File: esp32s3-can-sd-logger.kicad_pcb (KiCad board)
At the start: 4 copper layers, 84 x 100 mm, 206 parts, among them J1 PWR + CAN harness, J10 Sensor harness, J2 USB-C, J3 UART0, J4 I2C / Qwiic, J5 SPI, J6 WS2812, J7 Spare IO, J8 Rail break-out, J9 microSD push-pull, Q1 IPD068N10, Q2 AO3401A, Q3 2N7002, Q4 AO3401A, Q5 MMBT3906, Q6 DMG2301L, Q7 2N7002, SW1 RESET, SW2 BOOT, U1 LM74700-Q1, U10 SRV05-4, U11 SRV05-4, U12 TJA1051T/3, U13 ADS1115, U2 TLV431A, U3 LM5164 (5V), U4 LM5164 (3V3), U5 ESP32-S3-WROOM-1-N16R8, U6 TLV431A, U7 USBLC6-2SC6, U8 USBLC6-2SC6, U9 74AHCT1G125

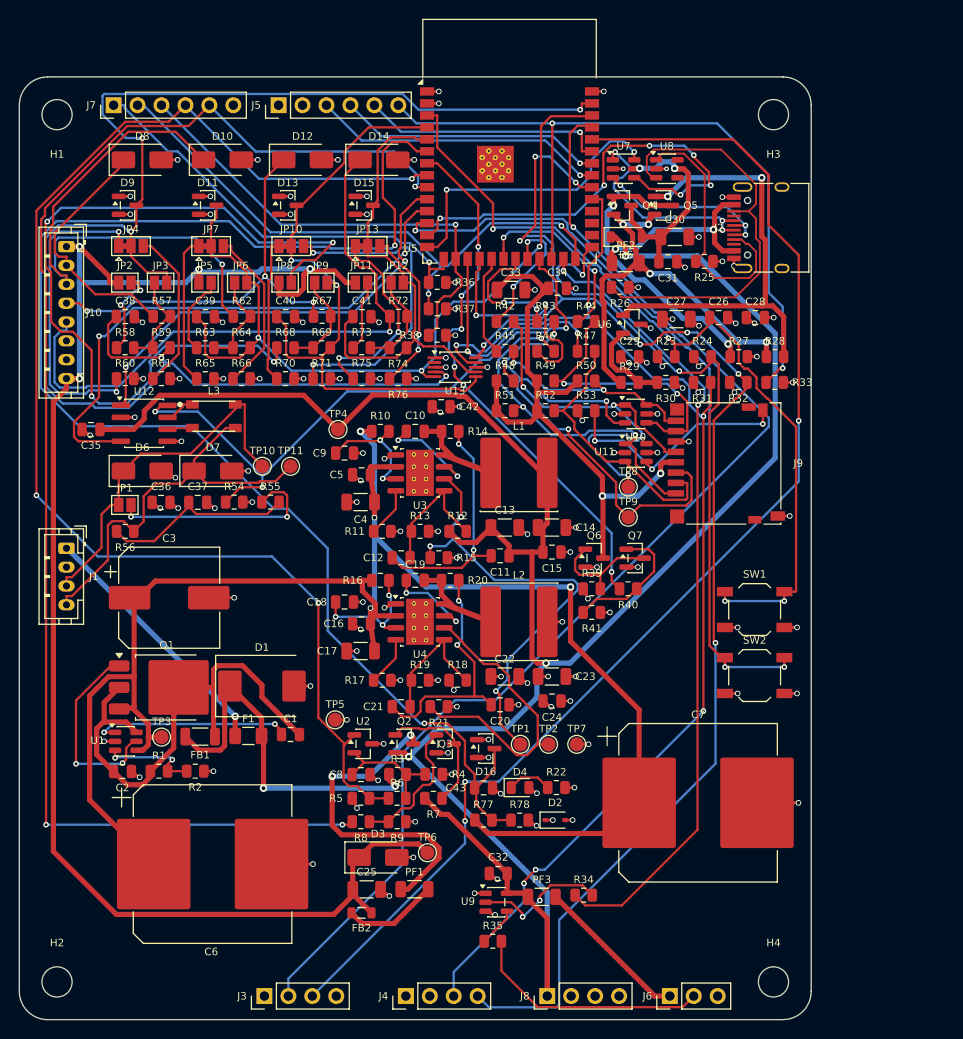
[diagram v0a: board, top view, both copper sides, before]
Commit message: Re-scope the fork as a carrier board: no power section, differential analog, K-line
The shield idea does not survive measurement. Component courtyard on the
parent is 3052 mm2 over an 84 x 100 board -- 36% packing, not the 50% I had
been estimating -- and a DevKitC-1 is 63 x 25.5 = 1607 mm2. The parts alone
were 1.4x the whole dev board. So this is a carrier the dev board plugs into,
not a shield that fits on top of one.

Power section deleted entirely. It was 1746 mm2, 57% of the board, for two
rails the DevKitC-1 already makes from its USB-C. Gone: both LM5164 bucks and
everything around them, the LM74700 ideal diode, the reverse-battery FET, the
three electrolytic cans, the 12 V input, and the sensor-rail load switch.
Both rails are now inputs, taken up through the sockets -- which reverses the
earlier "feed 5 V only" rule, because there is no longer a second regulator
to parallel against.

Hold-up is a supercapacitor, not electrolytics. The first sizing was wrong:
energy goes as V-squared and the usable window at 5 V is 4.2 -> 3.6 V, so
2000 uF buys 12.5 ms, not the ~50 ms claimed. 0.5 F over the same window is
2.5 s, in less area than one of the 100 V cans it replaces. Low-ESR
cylindrical cells specifically -- coin EDLCs are 30-200 ohm and cannot source
120 mA at all.

Analog runs differentially. The board is grounded twice now, through the
sensor loom and through USB by way of a charger elsewhere in the car, and a
few hundred mV of chassis drop is 6% of a 0-5 V channel -- which makes the
0.1% dividers pointless. The correction has to be at the divider, not the
ADC, so the sensor ground comes back as a Kelvin wire through a matched
attenuator. Two ADS1115s, because one MUX only offers three channels against
a shared negative.

K-line added, discrete rather than an L9637D: that part's TXD threshold is
0.7*VCC = 3.5 V and a 3.3 V GPIO cannot meet it. Low-side 2N7002, clamped
22k/10k receiver, optional ISO 9141 tester pull-up on a jumper.

Pin map regrouped by boa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
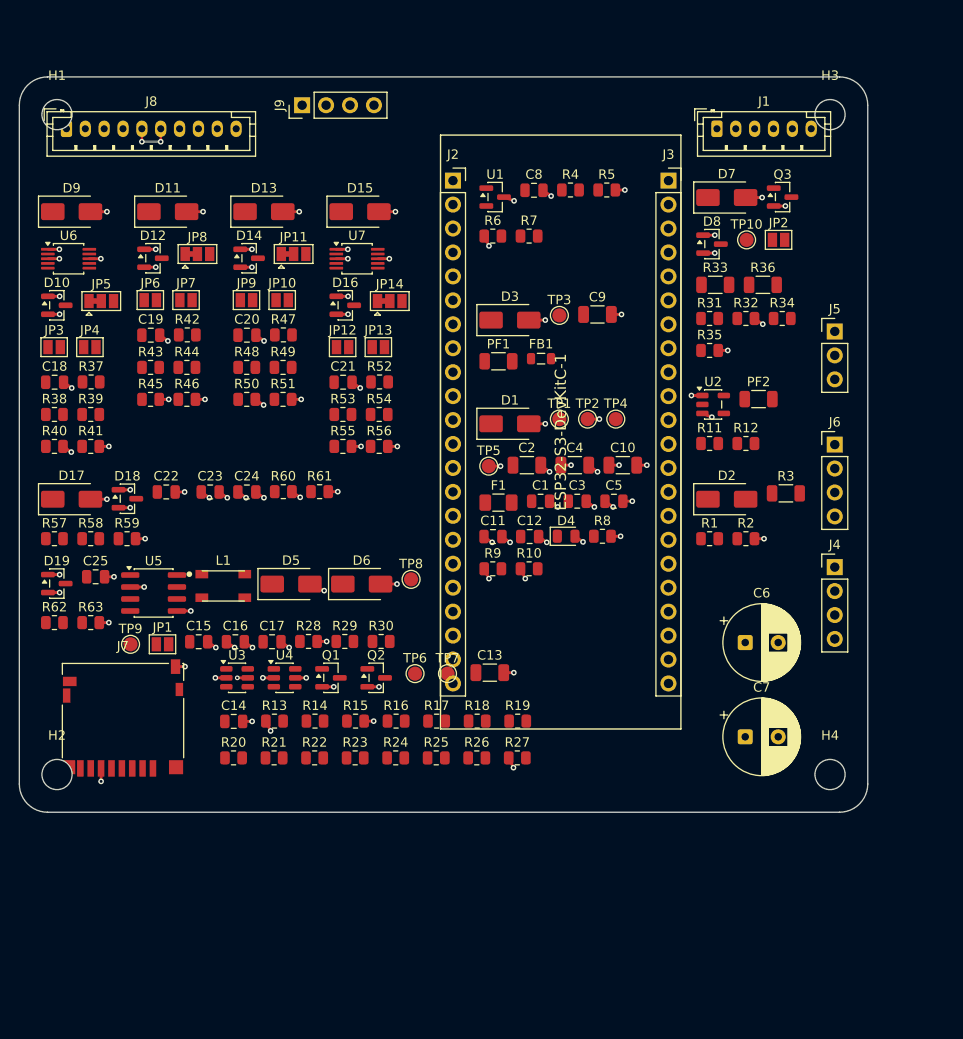
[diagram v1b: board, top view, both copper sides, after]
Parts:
- removed C26: 1uF, C_0805_2012Metric
- removed C27, C30, C33: 10uF, C_1206_3216Metric
- removed C28, C29, C31, C32, C34, C35, C36, C38, C39, C40, C41, C42, C43: 100nF, C_0805_2012Metric
- removed C37: 4.7nF, C_0805_2012Metric
- removed FB2: 600R, L_0805_2012Metric
- removed J10: Sensor harness, JST_PH_B8B-PH-K_1x08_P2.00mm_Vertical
- removed L2: 22uH, L_Sunlord_SWPA8040S
- removed L3: 51uH, L_CommonMode_TDK_ACT45B
- removed PF3: 0.5A hold, R_1206_3216Metric
- removed Q4: AO3401A, SOT-23
- removed Q5: MMBT3906, SOT-23
- removed Q6: DMG2301L, SOT-23
- removed Q7: 2N7002, SOT-23
- removed R64, R69, R74: 10k, R_0805_2012Metric
- removed R65, R70, R75: 15k, R_0805_2012Metric
- removed R66, R71, R76: 2.21k, R_0805_2012Metric
- removed R67, R72: 1k, R_0805_2012Metric
- removed R68, R73: 2.49k, R_0805_2012Metric
- removed R77: 100k, R_0805_2012Metric
- removed R78: 8.2k, R_0805_2012Metric
- removed SW1: RESET, SW_SPST_TL3342
- removed SW2: BOOT, SW_SPST_TL3342
- removed TP11: CAN_L, TestPoint_Pad_D1.5mm
- removed U10, U11: SRV05-4, SOT-23-6
- removed U12: TJA1051T/3, SOIC-8_3.9x4.9mm_P1.27mm
- removed U13: ADS1115, VSSOP-10_3x3mm_P0.5mm
- removed U8: USBLC6-2SC6, SOT-23-6
- removed U9: 74AHCT1G125, SOT-23-5
- added D17: SMAJ40CA, D_SMA, F.Cu at (5.54, 44.8)
- added D18: BAT54S, SOT-23, F.Cu at (11.5, 44.7)
- added D19: BAT54S, SOT-23, F.Cu at (3.98, 53.7)
- added JP14: RANGE4 (default 0-5V), SolderJumper-3_P1.3mm_Bridged12_Pad1.0x1.5mm, F.Cu at (39.3, 23.8)
- C1: value 1uF -> 100nF
- C10: value 2.2nF -> 10uF; footprint C_0805_2012Metric -> C_1206_3216Metric
- C11, C19, C20: value 2.2nF -> 100nF
- C12, C21: value 270pF -> 100nF
- C13: value 22uF -> 10uF
- C14, C22, C23: value 22uF -> 100nF; footprint C_1206_3216Metric -> C_0805_2012Metric
- C17: value 10uF -> 4.7nF; footprint C_1206_3216Metric -> C_0805_2012Metric
- C18: value 10nF -> 100nF
- C2: value 100nF -> 22uF; footprint C_0805_2012Metric -> C_1206_3216Metric
- C25: value 10uF -> 100nF; footprint C_1206_3216Metric -> C_0805_2012Metric
- C3: value 100uF -> 100nF; footprint CP_Elec_10x10.5 -> C_0805_2012Metric
- C4: value 10uF -> 22uF
- C6, C7: value 330uF -> 1F; footprint CP_Elec_16x22 -> CP_Radial_D8.0mm_P3.50mm
- C9: value 10nF -> 10uF; footprint C_0805_2012Metric -> C_1206_3216Metric
- D1: value SMCJ40CA -> SMAJ26CA; footprint D_SMC -> D_SMA
- D10, D12, D14, D8: value SMAJ40CA -> BAT54S; footprint D_SMA -> SOT-23
- D11, D13, D15, D9: value BAT54S -> SMAJ40CA; footprint SOT-23 -> D_SMA
- D2: value 3.6V 300mW -> SS14; footprint D_SOD-323 -> D_SMA
- D5: value 40V 1A -> SMAJ26CA; footprint D_SOD-123 -> D_SMA
- F1: value 2A slow -> 0.5A slow
- FB1: footprint L_1206_3216Metric -> L_0805_2012Metric
- J1: value PWR + CAN harness -> OBD-II harness; footprint JST_PH_B4B-PH-K_1x04_P2.00mm_Vertical -> JST_PH_B6B-PH-K_1x06_P2.00mm_Vertical
- J2: value USB-C -> DevKit J1; footprint USB_C_Receptacle_HRO_TYPE-C-31-M-12 -> PinSocket_1x22_P2.54mm_Vertical
- J3: value UART0 -> DevKit J3; footprint PinHeader_1x04_P2.54mm_Vertical -> PinSocket_1x22_P2.54mm_Vertical
- J5: value SPI -> WS2812; footprint PinHeader_1x06_P2.54mm_Vertical -> PinHeader_1x03_P2.54mm_Vertical
- J6: value WS2812 -> Rail break-out; footprint PinHeader_1x03_P2.54mm_Vertical -> PinHeader_1x04_P2.54mm_Vertical
- J7: value Spare IO -> microSD push-pull; footprint PinHeader_1x06_P2.54mm_Vertical -> microSD_HC_Hirose_DM3D-SF
- J8: value Rail break-out -> Sensor harness; footprint PinHeader_1x04_P2.54mm_Vertical -> JST_PH_B10B-PH-K_1x10_P2.00mm_Vertical
- J9: value microSD push-pull -> Spare diff in; footprint microSD_HC_Hirose_DM3D-SF -> PinHeader_1x04_P2.54mm_Vertical
- JP10: value RANGE3 (default 0-5V) -> BYPASS3; footprint SolderJumper-3_P1.3mm_Bridged12_Pad1.0x1.5mm -> SolderJumper-2_P1.3mm_Open_Pad1.0x1.5mm
- JP11: value PULLUP4 -> RANGE3 (default 0-5V); footprint SolderJumper-2_P1.3mm_Open_Pad1.0x1.5mm -> SolderJumper-3_P1.3mm_Bridged12_Pad1.0x1.5mm
- JP12: value BYPASS4 -> PULLUP4
- JP13: value RANGE4 (default 0-5V) -> BYPASS4; footprint SolderJumper-3_P1.3mm_Bridged12_Pad1.0x1.5mm -> SolderJumper-2_P1.3mm_Open_Pad1.0x1.5mm
- JP2: value PULLUP1 -> KPU (default OFF)
- JP3: value BYPASS1 -> PULLUP1
- JP4: value RANGE1 (default 0-5V) -> BYPASS1; footprint SolderJumper-3_P1.3mm_Bridged12_Pad1.0x1.5mm -> SolderJumper-2_P1.3mm_Open_Pad1.0x1.5mm
- JP5: value PULLUP2 -> RANGE1 (default 0-5V); footprint SolderJumper-2_P1.3mm_Open_Pad1.0x1.5mm -> SolderJumper-3_P1.3mm_Bridged12_Pad1.0x1.5mm
- JP6: value BYPASS2 -> PULLUP2
- JP7: value RANGE2 (default 0-5V) -> BYPASS2; footprint SolderJumper-3_P1.3mm_Bridged12_Pad1.0x1.5mm -> SolderJumper-2_P1.3mm_Open_Pad1.0x1.5mm
- JP8: value PULLUP3 -> RANGE2 (default 0-5V); footprint SolderJumper-2_P1.3mm_Open_Pad1.0x1.5mm -> SolderJumper-3_P1.3mm_Bridged12_Pad1.0x1.5mm
- JP9: value BYPASS3 -> PULLUP3
- L1: value 33uH -> 51uH; footprint L_Sunlord_SWPA8040S -> L_CommonMode_TDK_ACT45B
- Q1: value IPD068N10 -> DMG2301L; footprint TO-252-3_TabPin2 -> SOT-23
- Q2: value AO3401A -> 2N7002
- R10, R9: value 100k -> 4.7k
- R11: value 31.6k -> 33
- R12: value 100k -> 100
- R13: value 31.6k -> 100k
- R14: value 121k -> 1k
- R16, R18, R21: value 100k -> 33
- R17: value 20.5k -> 33
- R19: value 57.6k -> 33
- R2: value 44.2k -> 100k
- R20: value 95.3k -> 33
- R22: value 1k -> 10k
- R25, R26: value 5.1k -> 10k
- R27: value 100k -> 47k
- R29: value 100k -> 60.4
- R3: value 100k -> 22; footprint R_0805_2012Metric -> R_1206_3216Metric
- R30: value 27.4k -> 60.4
- R31: value 4.7k -> 10k
- R32: value 4.7k -> 100k
- R33: value 10k -> 33; footprint R_0805_2012Metric -> R_1206_3216Metric
- R34: value 33 -> 22k
- R35: value 100 -> 10k
- R36: value 10k -> 510; footprint R_0805_2012Metric -> R_1206_3216Metric
- R37, R52, R8: value 10k -> 1k
- R38, R48: value 10k -> 2.49k
- R39: value 100k -> 10k
- R4: value 12.7k -> 28.7k
- R40: value 1k -> 15k
- R41: value 100k -> 2.21k
- R42, R47: value 33 -> 1k
- R43: value 33 -> 2.49k
- R44: value 33 -> 10k
- R45: value 33 -> 15k
- R46: value 33 -> 2.21k
- R5: value 10k -> 12.0k
- R50, R59: value 10k -> 15k
- R51: value 10k -> 2.21k
- R53: value 47k -> 2.49k
- R55: value 60.4 -> 15k
- R56: value 60.4 -> 2.21k
- R58: value 2.49k -> 10k
- R6: value 1M -> 10k
- R60: value 15k -> 100k
- R61: value 2.21k -> 100k
- R62: value 1k -> 100k
- R63: value 2.49k -> 8.2k
- R7: value 100k -> 1M
- TP1: value PG_5V -> +5V
- TP10: value CAN_H -> K_LINE
- TP2: value PG_3V3 -> +3V3
- TP3: value +VBAT -> +5VS
- TP4: value +5V -> OBD_VBAT
- TP5: value +3V3 -> GND
- TP6: value +5VS -> SD_CLK
- TP7: value GND -> SD_CMD
- TP8: value SD_CLK -> CAN_H
- TP9: value SD_CMD -> CAN_L
- U1: value LM74700-Q1 -> TLV431A; footprint SOT-23-6 -> SOT-23
- U2: value TLV431A -> 74AHCT1G125; footprint SOT-23 -> SOT-23-5
- U3: value LM5164 (5V) -> SRV05-4; footprint SOIC-8-1EP_3.9x4.9mm_P1.27mm_EP2.95x4.9mm_Mask2.71x3.4mm_ThermalVias -> SOT-23-6
- U4: value LM5164 (3V3) -> SRV05-4; footprint SOIC-8-1EP_3.9x4.9mm_P1.27mm_EP2.95x4.9mm_Mask2.71x3.4mm_ThermalVias -> SOT-23-6
- U5: value ESP32-S3-WROOM-1-N16R8 -> TJA1051T/3; footprint ESP32-S3-WROOM-1 -> SOIC-8_3.9x4.9mm_P1.27mm
- U6: value TLV431A -> ADS1115 (0x48); footprint SOT-23 -> VSSOP-10_3x3mm_P0.5mm
- U7: value USBLC6-2SC6 -> ADS1115 (0x49); footprint SOT-23-6 -> VSSOP-10_3x3mm_P0.5mm
- moved J8 105.2 mm to (5.00, 5.50), turned to 0 degrees
- moved J3 96.5 mm to (68.9, 11.0), turned to 0 degrees
- moved J1 82.1 mm to (74.0, 5.50), turned to 0 degrees
- moved U1 69.8 mm to (50.5, 12.7)
- moved R5 69.6 mm to (62.3, 12.0)
- moved JP2 69.5 mm to (80.5, 17.3)
- moved Q3 68.2 mm to (81.0, 12.7)
- moved R35 66.8 mm to (73.2, 29.0)
- moved J7 65.0 mm to (11.0, 68.0), turned to 0 degrees
- moved R34 64.7 mm to (80.9, 25.6)
- moved C8 64.6 mm to (54.6, 12.0)
- moved J4 64.3 mm to (86.5, 52.0), turned to 0 degrees
- moved J5 63.7 mm to (86.5, 27.0), turned to 0 degrees
- moved R4 63.7 mm to (58.5, 12.0)
- moved R2 63.4 mm to (77.1, 49.0)
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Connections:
- C1 pad 1: VCAP -> OBD_VBAT_F
- C1 pad 2: VBAT_FB -> GND
- C10 pad 1: BST_5V -> +3V3
- C10 pad 2: SW_5V -> GND
- C11 pad 1: RAMP_5V -> +3V3
- C11 pad 2: +5V -> GND
- C12 pad 1: RAMP_5V -> +5V
- C12 pad 2: FB_5V -> GND
- C13 pad 1: +5V -> SD_VDD
- C14 pad 1: +5V -> SD_VDD
- C16 pad 1: +VBAT -> +3V3
- C17 pad 1: +VBAT -> CAN_SPLIT
- C18 pad 1: EN_3V3 -> AIN1
- C19 pad 1: BST_3V3 -> AIN2
- C19 pad 2: SW_3V3 -> GND
- C2 pad 1: VBAT_FB -> +5V
- C20 pad 1: RAMP_3V3 -> AIN3
- C20 pad 2: +3V3 -> GND
- C21 pad 1: RAMP_3V3 -> AIN4
- C21 pad 2: FB_3V3 -> GND
- C22 pad 1: +3V3 -> AGND_SENSE
- C25 pad 1: +5VS -> VBAT_SNS
- C3 pad 1: +VBAT -> +5V
- C4 pad 1: +VBAT -> +3V3
- C5 pad 1: +VBAT -> +3V3
- C6 pad 1: +VBAT -> SCAP_TOP
- C6 pad 2: GND -> SCAP_MID
- C7 pad 1: +VBAT -> SCAP_MID
- C9 pad 1: EN_5V -> +5VS
- D1 pad 1: VBAT_F -> OBD_VBAT_F
- D10 pad 1: AIN2_IN -> GND
- D10 pad 2: GND -> +3V3
- D11 pad 1: GND -> AIN2_IN
- D11 pad 2: +3V3 -> GND
- D12 pad 1: AIN3_IN -> GND
- D12 pad 2: GND -> +3V3
- D13 pad 1: GND -> AIN3_IN
- D13 pad 2: +3V3 -> GND
- D14 pad 1: AIN4_IN -> GND
- D14 pad 2: GND -> +3V3
- D15 pad 1: GND -> AIN4_IN
- D15 pad 2: +3V3 -> GND
- D16 pad 3: VBAT_SNS -> AIN4
- D2 pad 1: +3V3 -> SCAP_TOP
- D2 pad 2: GND -> +5V
- D5 pad 1: +5V -> CAN_H
- D5 pad 2: VBUS -> GND
- D6 pad 1: CAN_H -> CAN_L
- D7 pad 1: CAN_L -> K_LINE
- D8 pad 1: AIN1_IN -> GND
- D8 pad 2: GND -> +3V3
- D9 pad 1: GND -> AIN1_IN
- D9 pad 2: +3V3 -> GND
- F1 pad 1: VBAT_IN -> OBD_VBAT
- F1 pad 2: VBAT_F -> OBD_VBAT_F
- FB1 pad 1: VBAT_F -> VSENS_F
- FB1 pad 2: VBAT_FB -> +5VS
- J1 pad 1: VBAT_IN -> OBD_VBAT
- J3 pad 1: +3V3 -> GND
- J3 pad 2: UART_TX -> (no net)
- J3 pad 3: UART_RX -> (no net)
- J3 pad 4: GND -> (no net)
- J5 pad 1: +3V3 -> LED_5V
- J5 pad 2: GND -> LED_DIN_J
- J5 pad 3: SPI_SCK -> GND
- J6 pad 1: LED_5V -> +5V
- J6 pad 2: LED_DIN_J -> +3V3
- J7 pad 1: IO3 -> SD_D2_C
- J7 pad 2: IO45 -> SD_D3_C
- J7 pad 3: IO46 -> SD_CMD_C
- J7 pad 4: PWR_FAIL -> SD_VDD
- J7 pad 5: SENS_EN -> SD_CLK_C
- J8 pad 1: +5V -> +5VS
- J8 pad 2: +3V3 -> +5VS
- J8 pad 3: GND -> AIN1_IN
- J8 pad 4: GND -> AIN2_IN
- J9 pad 1: SD_D2_C -> AIN_SP1
- J9 pad 2: SD_D3_C -> AIN_SP2
- J9 pad 3: SD_CMD_C -> AGND_SENSE
- J9 pad 4: SD_VDD -> GND
- JP10 pad 1: AIN3_R1 -> AIN3_A
- JP11 pad 1: +5VS -> AIN3_R1
- JP11 pad 2: AIN4_PU -> AIN3
- JP12 pad 1: AIN4_A -> +5VS
- JP12 pad 2: AIN4 -> AIN4_PU
- JP13 pad 1: AIN4_R1 -> AIN4_A
- JP2 pad 1: +5VS -> OBD_VBAT_F
- JP2 pad 2: AIN1_PU -> K_PU
- JP3 pad 1: AIN1_A -> +5VS
- JP3 pad 2: AIN1 -> AIN1_PU
- JP4 pad 1: AIN1_R1 -> AIN1_A
- JP5 pad 1: +5VS -> AIN1_R1
- JP5 pad 2: AIN2_PU -> AIN1
- JP6 pad 1: AIN2_A -> +5VS
- JP6 pad 2: AIN2 -> AIN2_PU
- JP7 pad 1: AIN2_R1 -> AIN2_A
- JP8 pad 1: +5VS -> AIN2_R1
- JP8 pad 2: AIN3_PU -> AIN2
- JP9 pad 1: AIN3_A -> +5VS
- JP9 pad 2: AIN3 -> AIN3_PU
- L1 pad 1: SW_5V -> CANH_T
- L1 pad 2: +5V -> CAN_H
- PF1 pad 1: VSENS_SW -> +5V
- PF2 pad 1: VBUS_IN -> +5V
- PF2 pad 2: VBUS_R -> LED_5V
- Q1 pad 1: GATE_RB -> SD_PG
- Q1 pad 2: VBAT_FB -> +3V3
- Q1 pad 3: +VBAT -> SD_VDD
- Q2 pad 1: SENS_G -> SD_EN_G
- Q2 pad 2: +5V -> GND
- Q2 pad 3: VSENS_SW -> SD_PG
- Q3 pad 1: SENS_EN_G -> K_TX_G
- Q3 pad 3: SENS_G -> K_TX_D
- R1 pad 1: VBAT_FB -> SCAP_TOP
- R1 pad 2: VBAT_UVLO -> SCAP_MID
- R10 pad 1: +VBAT -> +3V3
- R10 pad 2: EN_5V -> I2C_SCL
- R11 pad 1: RON_5V -> LED_DIN_MCU
- R11 pad 2: GND -> LED_DIN_A
- R12 pad 1: +5V -> LED_DIN
- R12 pad 2: FB_5V -> LED_DIN_J
- R13 pad 1: FB_5V -> +3V3
- R13 pad 2: GND -> SD_PG
- R14 pad 1: SW_5V -> SD_PWR_EN
- R14 pad 2: RAMP_5V -> SD_EN_G
- R15 pad 1: PG_5V -> SD_EN_G
- R15 pad 2: +3V3 -> GND
- R16 pad 1: +VBAT -> SD_CLK
- R16 pad 2: EN_3V3 -> SD_CLK_C
- R17 pad 1: RON_3V3 -> SD_CMD
- R17 pad 2: GND -> SD_CMD_C
- R18 pad 1: +3V3 -> SD_D0
- R18 pad 2: FB_3V3 -> SD_D0_C
- R19 pad 1: FB_3V3 -> SD_D1
- R19 pad 2: GND -> SD_D1_C
- R2 pad 1: VBAT_UVLO -> SCAP_MID
- R20 pad 1: SW_3V3 -> SD_D2
- R20 pad 2: RAMP_3V3 -> SD_D2_C
- R21 pad 1: PG_3V3 -> SD_D3
- R21 pad 2: +3V3 -> SD_D3_C
- R22 pad 1: PWR_LED_K -> SD_VDD
- R22 pad 2: GND -> SD_CMD_C
- R23 pad 1: +3V3 -> SD_VDD
- R23 pad 2: MCU_EN -> SD_D0_C
- R24 pad 1: +3V3 -> SD_VDD
- R24 pad 2: MCU_BOOT -> SD_D1_C
- R25 pad 1: USB_CC1 -> SD_VDD
- R25 pad 2: GND -> SD_D2_C
- R26 pad 1: USB_CC2 -> SD_VDD
- R26 pad 2: GND -> SD_D3_C
- R27 pad 1: VBUS_G -> +3V3
- R27 pad 2: GND -> SD_CD
- R28 pad 1: VBUS_R -> CAN_S
- R28 pad 2: VBUS_OV -> GND
- R29 pad 1: VBUS_R -> TERM_A
- R29 pad 2: VBUS_OVS -> CAN_SPLIT
- R3 pad 1: VBAT_F -> +5V
- R3 pad 2: PFD_SENSE -> SCAP_TOP
- R30 pad 1: VBUS_OVS -> CAN_SPLIT
- R30 pad 2: GND -> CAN_L
- R31 pad 1: +3V3 -> K_TX
- R31 pad 2: I2C_SDA -> K_TX_G
- R32 pad 1: +3V3 -> K_TX_G
- R32 pad 2: I2C_SCL -> GND
- R33 pad 1: SPI_CS -> K_TX_D
- R33 pad 2: +3V3 -> K_LINE
- R34 pad 1: LED_DIN_MCU -> K_LINE
- R34 pad 2: LED_DIN_A -> K_RX
- R35 pad 1: LED_DIN -> K_RX
- R35 pad 2: LED_DIN_J -> GND
- R36 pad 1: IO3 -> K_PU
- R36 pad 2: GND -> K_LINE
- R37 pad 1: IO45 -> AIN1_IN
- R37 pad 2: GND -> AIN1_A
- R38 pad 1: IO46 -> AIN1_PU
- R38 pad 2: GND -> AIN1_A
- R39 pad 1: +3V3 -> AIN1_A
- R39 pad 2: SD_PG -> AIN1
- R4 pad 1: PFD_SENSE -> +5V
- R4 pad 2: GND -> PFD_SENSE
- R40 pad 1: SD_PWR_EN -> AIN1_R1
- R40 pad 2: SD_EN_G -> GND
- R41 pad 1: SD_EN_G -> AIN1_R2
- R42 pad 1: SD_CLK -> AIN2_IN
- R42 pad 2: SD_CLK_C -> AIN2_A
- R43 pad 1: SD_CMD -> AIN2_PU
- R43 pad 2: SD_CMD_C -> AIN2_A
- R44 pad 1: SD_D0 -> AIN2_A
- R44 pad 2: SD_D0_C -> AIN2
- R45 pad 1: SD_D1 -> AIN2_R1
- R45 pad 2: SD_D1_C -> GND
- R46 pad 1: SD_D2 -> AIN2_R2
- R46 pad 2: SD_D2_C -> GND
- R47 pad 1: SD_D3 -> AIN3_IN
- R47 pad 2: SD_D3_C -> AIN3_A
- R48 pad 1: SD_VDD -> AIN3_PU
- R48 pad 2: SD_CMD_C -> AIN3_A
- R49 pad 1: SD_VDD -> AIN3_A
- R49 pad 2: SD_D0_C -> AIN3
- R5 pad 1: +3V3 -> PFD_SENSE
- R5 pad 2: PWR_FAIL -> GND
- R50 pad 1: SD_VDD -> AIN3_R1
- R50 pad 2: SD_D1_C -> GND
- R51 pad 1: SD_VDD -> AIN3_R2
- R51 pad 2: SD_D2_C -> GND
- R52 pad 1: SD_VDD -> AIN4_IN
- R52 pad 2: SD_D3_C -> AIN4_A
- R53 pad 1: +3V3 -> AIN4_PU
- R53 pad 2: SD_CD -> AIN4_A
- R54 pad 1: CAN_S -> AIN4_A
- R54 pad 2: GND -> AIN4
- R55 pad 1: TERM_A -> AIN4_R1
- R55 pad 2: CAN_SPLIT -> GND
- R56 pad 1: CAN_SPLIT -> AIN4_R2
- R56 pad 2: CAN_L -> GND
- R57 pad 1: AIN1_IN -> SENS_RTN
- R57 pad 2: AIN1_A -> AGND_A
- R58 pad 1: AIN1_PU -> AGND_A
- R58 pad 2: AIN1_A -> AGND_SENSE
- R59 pad 1: AIN1_A -> AGND_SENSE
- R59 pad 2: AIN1 -> GND
- R6 pad 1: PWR_FAIL -> +3V3
- R6 pad 2: PFD_SENSE -> PWR_FAIL
- R60 pad 1: AIN1_R1 -> AIN_SP1
- R61 pad 1: AIN1_R2 -> AIN_SP2
- R62 pad 1: AIN2_IN -> OBD_VBAT
- R62 pad 2: AIN2_A -> VBAT_SNS
- R63 pad 1: AIN2_PU -> VBAT_SNS
- R63 pad 2: AIN2_A -> GND
- R7 pad 1: +5V -> PWR_FAIL
- R7 pad 2: SENS_G -> PFD_SENSE
- R8 pad 1: SENS_EN -> PWR_LED_K
- R8 pad 2: SENS_EN_G -> GND
- R9 pad 1: SENS_EN_G -> +3V3
- R9 pad 2: GND -> I2C_SDA
- TP1 pad 1: PG_5V -> +5V
- TP10 pad 1: CAN_H -> K_LINE
- TP2 pad 1: PG_3V3 -> +3V3
- TP3 pad 1: +VBAT -> +5VS
- TP4 pad 1: +5V -> OBD_VBAT
- TP5 pad 1: +3V3 -> GND
- TP6 pad 1: +5VS -> SD_CLK_C
- TP7 pad 1: GND -> SD_CMD_C
- TP8 pad 1: SD_CLK_C -> CAN_H
- TP9 pad 1: SD_CMD_C -> CAN_L
- U1 pad 1: VCAP -> PWR_FAIL
- U1 pad 2: GND -> PFD_SENSE
- U1 pad 3: VBAT_UVLO -> GND
- U2 pad 1: PWR_FAIL -> GND
- U2 pad 2: PFD_SENSE -> LED_DIN_A
- U3 pad 1: GND -> SD_CLK_C
- U3 pad 2: +VBAT -> GND
- U3 pad 3: EN_5V -> SD_CMD_C
- U3 pad 4: RON_5V -> SD_D0_C
- U3 pad 5: FB_5V -> +3V3
- U3 pad 6: PG_5V -> SD_D1_C
- U4 pad 1: GND -> SD_D2_C
- U4 pad 2: +VBAT -> GND
- U4 pad 3: EN_3V3 -> SD_D3_C
- U4 pad 4: RON_3V3 -> SD_CD
- U4 pad 5: FB_3V3 -> +3V3
- U4 pad 6: PG_3V3 -> (no net)
- U5 pad 1: GND -> CAN_TX
- U5 pad 2: +3V3 -> GND
- U5 pad 3: MCU_EN -> +5V
- U5 pad 4: AIN3 -> CAN_RX
- U5 pad 5: AIN4 -> +3V3
- U5 pad 6: VBAT_SNS -> CANL_T
- U5 pad 7: SD_PWR_EN -> CANH_T
- U5 pad 8: PWR_FAIL -> CAN_S
- U6 pad 1: VBUS_OV -> GND
- U6 pad 2: VBUS_OVS -> (no net)
- U7 pad 1: USB_DP_CON -> +3V3
- U7 pad 2: GND -> (no net)
- U7 pad 3: USB_DM_CON -> GND
- U7 pad 4: USB_DM -> AIN4
- U7 pad 5: VBUS -> AIN_SP1
- U7 pad 6: USB_DP -> AIN_SP2
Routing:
- net +5V: track 241.0 -> 0.00 mm, vias 3 -> 0
- net +VBAT: track 183.1 -> 0.00 mm, vias 4 -> 0
- net AIN1: track 165.7 -> 0.00 mm, vias 5 -> 0
- net +5VS: track 162.9 -> 0.00 mm, vias 4 -> 0
- net VBAT_SNS: track 153.9 -> 0.00 mm, vias 2 -> 0
- net SENS_EN: track 148.2 -> 0.00 mm, vias 3 -> 0
- net I2C_SCL: track 147.4 -> 0.00 mm, vias 8 -> 0
- net PWR_FAIL: track 141.3 -> 0.00 mm, vias 3 -> 0
- net UART_RX: track 132.2 -> 0.00 mm, vias 3 -> 0
- net I2C_SDA: track 127.8 -> 0.00 mm, vias 6 -> 0
- net UART_TX: track 127.2 -> 0.00 mm, vias 1 -> 0
- net MCU_EN: track 89.7 -> 0.00 mm, vias 4 -> 0
- net AIN2: track 88.7 -> 0.00 mm, vias 3 -> 0
- net AIN3_PU: track 86.4 -> 0.00 mm, vias 4 -> 0
- net LED_DIN_MCU: track 85.3 -> 0.00 mm, vias 2 -> 0
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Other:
- board size 84 x 100 mm -> 90 x 78 mm
- board text added: "ESP32-S3-DevKitC-1"

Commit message: Second CAN bus, single analog range, and three placement bugs the render caught
TWO CAN BUSES AT ONCE NEEDS A SECOND CONTROLLER. The ESP32-S3 has exactly
one TWAI peripheral. Two transceivers on it would give a bus you can pick at
runtime through the GPIO matrix, never two live at once, and the point of a
second bus is watching the powertrain and the body bus together. So the
second channel is an MCP2518FD on SPI (SOIC-14, KiCad ships the pin-compatible
MCP2517FD symbol) with its own 40 MHz crystal, its own TJA1051 -- same part
as CAN 1, so two positions on one BOM line -- choke, split termination and
clamps.

That cost five pins against two spare. The three came from dropping the
microSD to 1-bit SDMMC, which measurement says is free: the busiest case this
logger will see is ~128 kB/s against 1-bit's ~1500 kB/s, and bus width does
not touch the card's internal write stall, which is the only thing the
hold-up budget is actually sized around. The card keeps its D1/D2/D3
pull-ups because a card samples DAT3 at power-up and drops into SPI mode if
it finds it low -- they simply stop at the socket now.

Jumpers on the aux harness pins pick K-line or the second CAN pair, because
those two genuinely cannot share a wire: K-line idles at battery voltage and
a CAN transceiver biases its bus to 2.5 V. The clamps sit ahead of the
jumpers so the protection is the same either way, which also let the K-line
drop its own TVS. Default is K-line, which is what an R53 wants.

ANALOG DOWN TO ONE RANGE. The bypass and range-select jumpers are gone --
twelve jumpers and four resistors -- and every channel is a fixed 2.21/13.21
divider spanning 0-16 V, so a 5 V and a 12 V sensor both fit without
touching anything. Resolution was never the reason for a narrower range: a
5 V sensor lands at 0.836 V, which on a 16-bit ADS1115 is 6688 counts.

The real reason is the differential ground. A channel switched to 0-16 V
while the shared return attenuator stayed at the 0-5 V ratio subtracts
0.5769*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
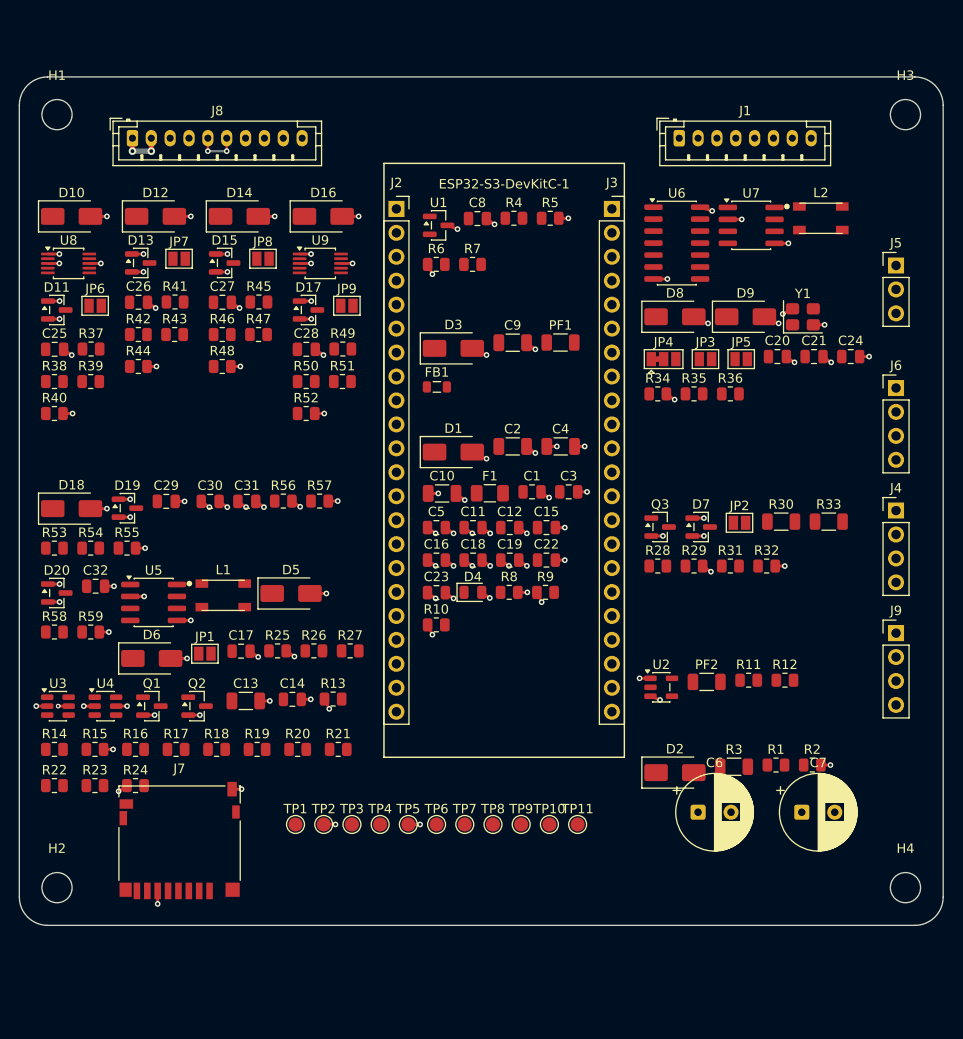
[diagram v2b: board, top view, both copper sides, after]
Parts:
- removed JP10: BYPASS3, SolderJumper-2_P1.3mm_Open_Pad1.0x1.5mm
- removed JP11: RANGE3 (default 0-5V), SolderJumper-3_P1.3mm_Bridged12_Pad1.0x1.5mm
- removed JP12: PULLUP4, SolderJumper-2_P1.3mm_Open_Pad1.0x1.5mm
- removed JP13: BYPASS4, SolderJumper-2_P1.3mm_Open_Pad1.0x1.5mm
- removed JP14: RANGE4 (default 0-5V), SolderJumper-3_P1.3mm_Bridged12_Pad1.0x1.5mm
- removed R60, R61, R62: 100k, R_0805_2012Metric
- removed R63: 8.2k, R_0805_2012Metric
- added C26: 100nF, C_0805_2012Metric, F.Cu at (12.6, 23.9)
- added C27: 100nF, C_0805_2012Metric, F.Cu at (21.5, 23.9)
- added C28: 100nF, C_0805_2012Metric, F.Cu at (30.4, 28.9)
- added C29: 100nF, C_0805_2012Metric, F.Cu at (15.6, 45.0)
- added C30: 100nF, C_0805_2012Metric, F.Cu at (20.2, 45.0)
- added C31: 100nF, C_0805_2012Metric, F.Cu at (24.1, 45.0)
- added C32: 100nF, C_0805_2012Metric, F.Cu at (8.10, 54.0)
- added D20: BAT54S, SOT-23, F.Cu at (3.98, 54.7)
- added L2: 51uH, L_CommonMode_TDK_ACT45B, F.Cu at (85.0, 15.0)
- added TP11: AUX_A, TestPoint_Pad_D1.5mm, F.Cu at (59.2, 79.3)
- added U8: ADS1115 (0x48), VSSOP-10_3x3mm_P0.5mm, F.Cu at (5.22, 19.8)
- added U9: ADS1115 (0x49), VSSOP-10_3x3mm_P0.5mm, F.Cu at (31.9, 19.8)
- added Y1: 40MHz, Crystal_SMD_3225-4Pin_3.2x2.5mm, F.Cu at (83.1, 25.4)
- C19: value 100nF -> 1uF
- C20, C21: value 100nF -> 15pF
- C24: value 100nF -> 4.7nF
- D10, D12, D14, D16, D18: value BAT54S -> SMAJ40CA; footprint SOT-23 -> D_SMA
- D11, D13, D15, D17: value SMAJ40CA -> BAT54S; footprint D_SMA -> SOT-23
- D7: value SMAJ26CA -> BAT54S; footprint D_SMA -> SOT-23
- D8: value BAT54S -> SMAJ26CA; footprint SOT-23 -> D_SMA
- D9: value SMAJ40CA -> SMAJ26CA
- J1: footprint JST_PH_B6B-PH-K_1x06_P2.00mm_Vertical -> JST_PH_B8B-PH-K_1x08_P2.00mm_Vertical
- JP3: value PULLUP1 -> TERM2 (default OFF)
- JP4: value BYPASS1 -> AUXSEL (default K-line); footprint SolderJumper-2_P1.3mm_Open_Pad1.0x1.5mm -> SolderJumper-3_P1.3mm_Bridged12_Pad1.0x1.5mm
- JP5: value RANGE1 (default 0-5V) -> AUXCL (default OFF); footprint SolderJumper-3_P1.3mm_Bridged12_Pad1.0x1.5mm -> SolderJumper-2_P1.3mm_Open_Pad1.0x1.5mm
- JP6: value PULLUP2 -> PULLUP1
- JP7: value BYPASS2 -> PULLUP2
- JP8: value RANGE2 (default 0-5V) -> PULLUP3; footprint SolderJumper-3_P1.3mm_Bridged12_Pad1.0x1.5mm -> SolderJumper-2_P1.3mm_Open_Pad1.0x1.5mm
- JP9: value PULLUP3 -> PULLUP4
- R19, R20, R21: value 33 -> 10k
- R24: value 10k -> 47k
- R26, R35: value 10k -> 60.4
- R27: value 47k -> 60.4
- R29: value 60.4 -> 100k
- R30: value 60.4 -> 33; footprint R_0805_2012Metric -> R_1206_3216Metric
- R31: value 10k -> 22k
- R32: value 100k -> 10k
- R33: value 33 -> 510
- R34: value 22k -> 10k
- R36: value 510 -> 60.4; footprint R_1206_3216Metric -> R_0805_2012Metric
- R40, R55: value 15k -> 2.21k
- R41: value 2.21k -> 1k
- R42: value 1k -> 2.49k
- R43: value 2.49k -> 10k
- R44: value 10k -> 2.21k
- R45: value 15k -> 1k
- R46: value 2.21k -> 2.49k
- R47: value 1k -> 10k
- R48: value 2.49k -> 2.21k
- R49: value 10k -> 1k
- R50: value 15k -> 2.49k
- R51: value 2.21k -> 10k
- R52: value 1k -> 2.21k
- R53: value 2.49k -> 1k
- R56: value 2.21k -> 100k
- R57: value 1k -> 100k
- R58: value 10k -> 100k
- R59: value 15k -> 8.2k
- U6: value ADS1115 (0x48) -> MCP2518FD; footprint VSSOP-10_3x3mm_P0.5mm -> SOIC-14_3.9x8.7mm_P1.27mm
- U7: value ADS1115 (0x49) -> TJA1051T/3; footprint VSSOP-10_3x3mm_P0.5mm -> SOIC-8_3.9x4.9mm_P1.27mm
- moved J9 84.3 mm to (93.0, 59.0), turned to 0 degrees
- moved D9 72.4 mm to (77.0, 25.4)
- moved JP3 69.1 mm to (72.8, 29.9)
- moved JP5 68.2 mm to (76.6, 29.9)
- moved C24 65.6 mm to (88.2, 29.7)
- moved TP10 65.4 mm to (56.2, 79.3)
- moved U6 64.5 mm to (69.7, 17.6)
- moved JP4 60.9 mm to (68.3, 29.9)
- moved TP3 58.3 mm to (35.3, 79.3)
- moved C20 56.3 mm to (80.4, 29.7)
- moved TP1 51.3 mm to (29.3, 79.3)
- moved TP2 51.3 mm to (32.3, 79.3)
- moved C21 50.0 mm to (84.3, 29.7)
- moved TP4 49.7 mm to (38.3, 79.3)
- moved C18 48.2 mm to (48.1, 51.3)
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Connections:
- C18 pad 1: AIN1 -> +3V3
- C19 pad 1: AIN2 -> +3V3
- C20 pad 1: AIN3 -> XTAL1
- C21 pad 1: AIN4 -> XTAL2
- C22 pad 1: AGND_SENSE -> +5V
- C24 pad 1: +3V3 -> CAN2_SPLIT
- C25 pad 1: VBAT_SNS -> AIN1
- D10 pad 1: GND -> AIN1_IN
- D10 pad 2: +3V3 -> GND
- D11 pad 1: AIN2_IN -> GND
- D11 pad 2: GND -> +3V3
- D12 pad 1: GND -> AIN2_IN
- D12 pad 2: +3V3 -> GND
- D13 pad 1: AIN3_IN -> GND
- D13 pad 2: GND -> +3V3
- D14 pad 1: GND -> AIN3_IN
- D14 pad 2: +3V3 -> GND
- D15 pad 1: AIN4_IN -> GND
- D15 pad 2: GND -> +3V3
- D16 pad 1: GND -> AIN4_IN
- D16 pad 2: +3V3 -> GND
- D17 pad 1: SENS_RTN -> GND
- D17 pad 2: GND -> +3V3
- D18 pad 1: GND -> SENS_RTN
- D18 pad 2: +3V3 -> GND
- D19 pad 3: VBAT_SNS -> AGND_SENSE
- D7 pad 1: K_LINE -> GND
- D7 pad 2: GND -> +3V3
- D8 pad 1: GND -> AUX_A
- D8 pad 2: +3V3 -> GND
- D9 pad 1: AIN1_IN -> AUX_B
- J1 pad 5: K_LINE -> AUX_A
- J1 pad 6: GND -> AUX_B
- J2 pad 15: SD_D3 -> I2C_SCL
- J2 pad 16: SD_D2 -> I2C_SDA
- J2 pad 17: SD_D1 -> SD_CD
- J3 pad 17: I2C_SDA -> SD_PWR_EN
- J3 pad 18: SD_CD -> CAN2_INT
- J3 pad 4: (no net) -> K_RX
- J3 pad 5: (no net) -> K_TX
- J3 pad 6: K_RX -> CAN2_CS
- J3 pad 7: K_TX -> CAN2_MISO
- J3 pad 8: SD_PWR_EN -> CAN2_MOSI
- J3 pad 9: I2C_SCL -> CAN2_SCK
- JP3 pad 1: +5VS -> CAN2_H_C
- JP3 pad 2: AIN1_PU -> TERM2_A
- JP4 pad 1: AIN1_A -> K_LINE
- JP4 pad 2: AIN1 -> AUX_A
- JP5 pad 1: AIN1_R1 -> AUX_B
- JP5 pad 2: AIN1 -> CAN2_L_C
- JP6 pad 2: AIN2_PU -> AIN1_PU
- JP7 pad 1: AIN2_A -> +5VS
- JP7 pad 2: AIN2 -> AIN2_PU
- JP8 pad 1: AIN2_R1 -> +5VS
- JP8 pad 2: AIN2 -> AIN3_PU
- JP9 pad 2: AIN3_PU -> AIN4_PU
- R19 pad 1: SD_D1 -> SD_VDD
- R19 pad 2: SD_D1_C -> SD_CMD_C
- R20 pad 1: SD_D2 -> SD_VDD
- R20 pad 2: SD_D2_C -> SD_D0_C
- R21 pad 1: SD_D3 -> SD_VDD
- R21 pad 2: SD_D3_C -> SD_D1_C
- R22 pad 2: SD_CMD_C -> SD_D2_C
- R23 pad 2: SD_D0_C -> SD_D3_C
- R24 pad 1: SD_VDD -> +3V3
- R24 pad 2: SD_D1_C -> SD_CD
- R25 pad 1: SD_VDD -> CAN_S
- R25 pad 2: SD_D2_C -> GND
- R26 pad 1: SD_VDD -> TERM_A
- R26 pad 2: SD_D3_C -> CAN_SPLIT
- R27 pad 1: +3V3 -> CAN_SPLIT
- R27 pad 2: SD_CD -> CAN_L
- R28 pad 1: CAN_S -> K_TX
- R28 pad 2: GND -> K_TX_G
- R29 pad 1: TERM_A -> K_TX_G
- R29 pad 2: CAN_SPLIT -> GND
- R30 pad 1: CAN_SPLIT -> K_TX_D
- R30 pad 2: CAN_L -> K_LINE
- R31 pad 1: K_TX -> K_LINE
- R31 pad 2: K_TX_G -> K_RX
- R32 pad 1: K_TX_G -> K_RX
- R33 pad 1: K_TX_D -> K_PU
- R34 pad 1: K_LINE -> CAN2_S
- R34 pad 2: K_RX -> GND
- R35 pad 1: K_RX -> TERM2_A
- R35 pad 2: GND -> CAN2_SPLIT
- R36 pad 1: K_PU -> CAN2_SPLIT
- R36 pad 2: K_LINE -> CAN2_L_C
- R40 pad 1: AIN1_R1 -> AIN1
- R41 pad 1: AIN1_R2 -> AIN2_IN
- R41 pad 2: GND -> AIN2_A
- R42 pad 1: AIN2_IN -> AIN2_PU
- R43 pad 1: AIN2_PU -> AIN2_A
- R43 pad 2: AIN2_A -> AIN2
- R44 pad 1: AIN2_A -> AIN2
- R44 pad 2: AIN2 -> GND
- R45 pad 1: AIN2_R1 -> AIN3_IN
- R45 pad 2: GND -> AIN3_A
- R46 pad 1: AIN2_R2 -> AIN3_PU
- R46 pad 2: GND -> AIN3_A
- R47 pad 1: AIN3_IN -> AIN3_A
- R47 pad 2: AIN3_A -> AIN3
- R48 pad 1: AIN3_PU -> AIN3
- R48 pad 2: AIN3_A -> GND
- R49 pad 1: AIN3_A -> AIN4_IN
- R49 pad 2: AIN3 -> AIN4_A
- R50 pad 1: AIN3_R1 -> AIN4_PU
- R50 pad 2: GND -> AIN4_A
- R51 pad 1: AIN3_R2 -> AIN4_A
- R51 pad 2: GND -> AIN4
- R52 pad 1: AIN4_IN -> AIN4
- R52 pad 2: AIN4_A -> GND
- R53 pad 1: AIN4_PU -> SENS_RTN
- R53 pad 2: AIN4_A -> AGND_A
- R54 pad 1: AIN4_A -> AGND_A
- R54 pad 2: AIN4 -> AGND_SENSE
- R55 pad 1: AIN4_R1 -> AGND_SENSE
- R56 pad 1: AIN4_R2 -> AIN_SP1
- R57 pad 1: SENS_RTN -> AIN_SP2
- R57 pad 2: AGND_A -> GND
- R58 pad 1: AGND_A -> OBD_VBAT
- R58 pad 2: AGND_SENSE -> VBAT_SNS
- R59 pad 1: AGND_SENSE -> VBAT_SNS
- U6 pad 1: GND -> CAN2_TXD
- U6 pad 10: I2C_SCL -> CAN2_SCK
- U6 pad 2: (no net) -> CAN2_RXD
- U6 pad 3: GND -> (no net)
- U6 pad 4: AIN1 -> CAN2_INT
- U6 pad 5: AIN2 -> XTAL2
- U6 pad 6: AIN3 -> XTAL1
- U6 pad 7: AGND_SENSE -> GND
- U6 pad 8: +3V3 -> (no net)
- U6 pad 9: I2C_SDA -> (no net)
- U7 pad 1: +3V3 -> CAN2_TXD
- U7 pad 2: (no net) -> GND
- U7 pad 3: GND -> +5V
- U7 pad 4: AIN4 -> CAN2_RXD
- U7 pad 5: AIN_SP1 -> +3V3
- U7 pad 6: AIN_SP2 -> CAN2L_T
- U7 pad 7: AGND_SENSE -> CAN2H_T
- U7 pad 8: +3V3 -> CAN2_S
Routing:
- net GND: track 86.9 -> 98.0 mm, vias 73 -> 82
- net +3V3: track 32.9 -> 38.8 mm, vias 28 -> 33
- net +5VS: track 0.00 -> 4.75 mm, vias 0 -> 2
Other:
- board size 90 x 78 mm -> 98 x 90 mm
